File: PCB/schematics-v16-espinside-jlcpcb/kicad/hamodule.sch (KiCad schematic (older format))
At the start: 78 parts, among them J1 2604-1104, J10 EspSense, J11 Conn_01x02_Male, J2 2604-1102, J3 USB_B_Micro, J4 ESP Relays, J5 Current Jumper, J6 GND 3.3V, J7 Conn_01x02, J8 Current Jumper, J9 2604-1104, K1 PCN-105D, K2 PCN-105D, K3 PCN-105D, K4 PCN-105D, Q1 SS8050, Q2 SS8050, SW1 EN, SW2 IO0, U1 ULN2003A, U2 ESP32-WROOM-32D, U4 LD1117AV33_TO220, U5 MCP9700T-ETT, U6 LDA210-PDIP, U7 LDA210-PDIP, U8 CP2102N-A01-GQFN28

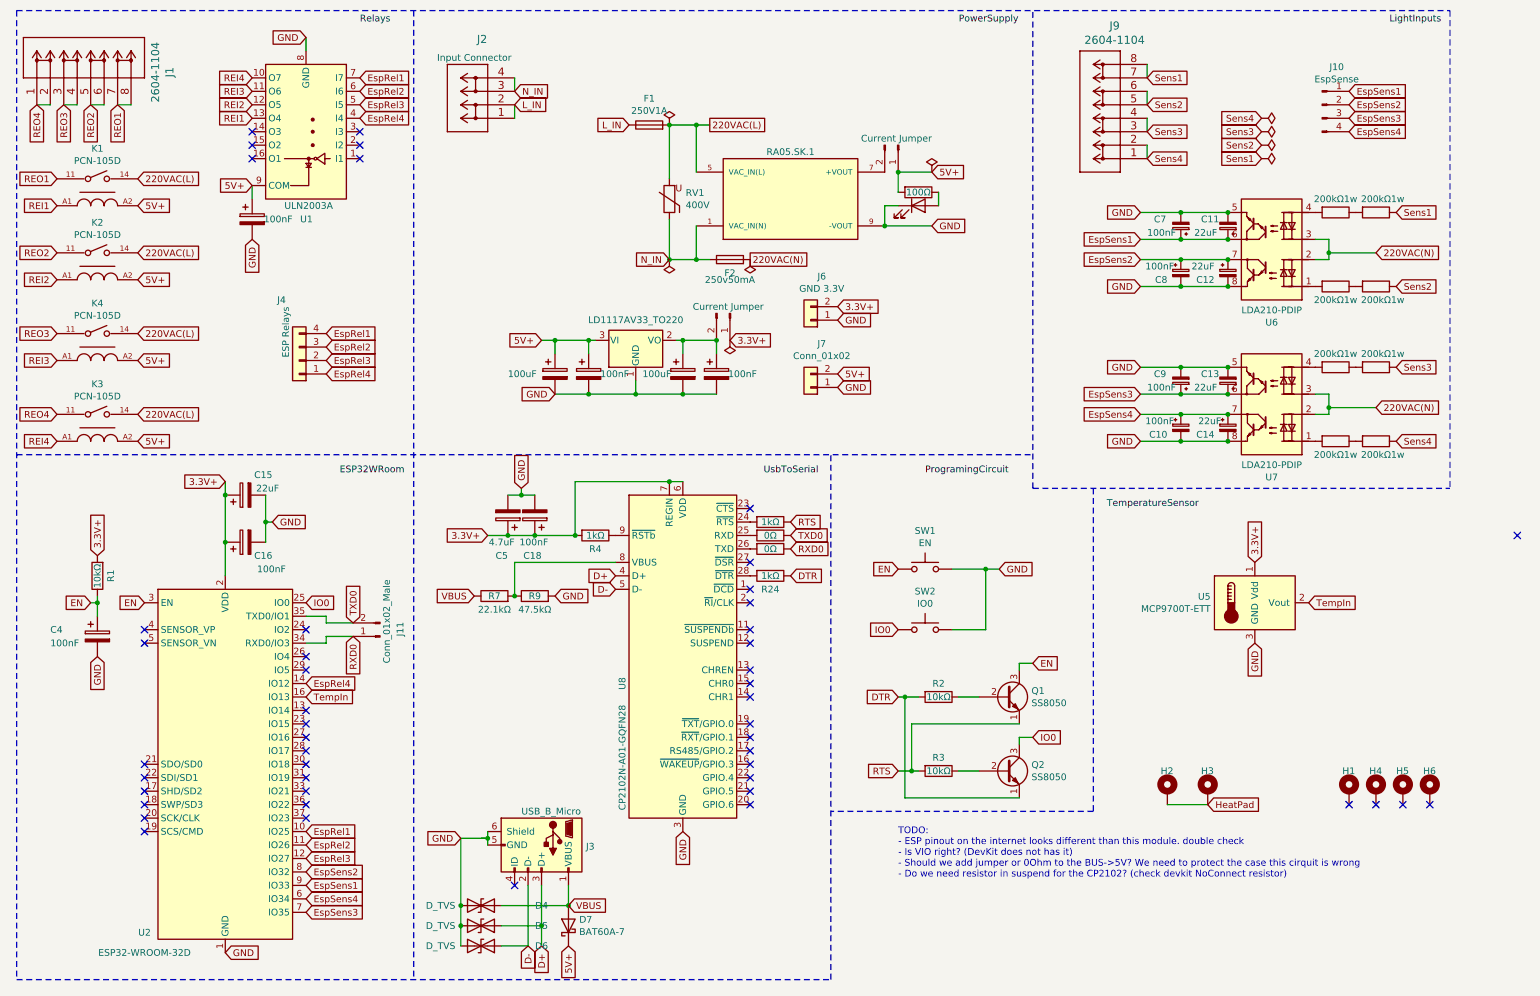
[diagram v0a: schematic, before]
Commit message: changed big caps + readme + routing + JLCPCB
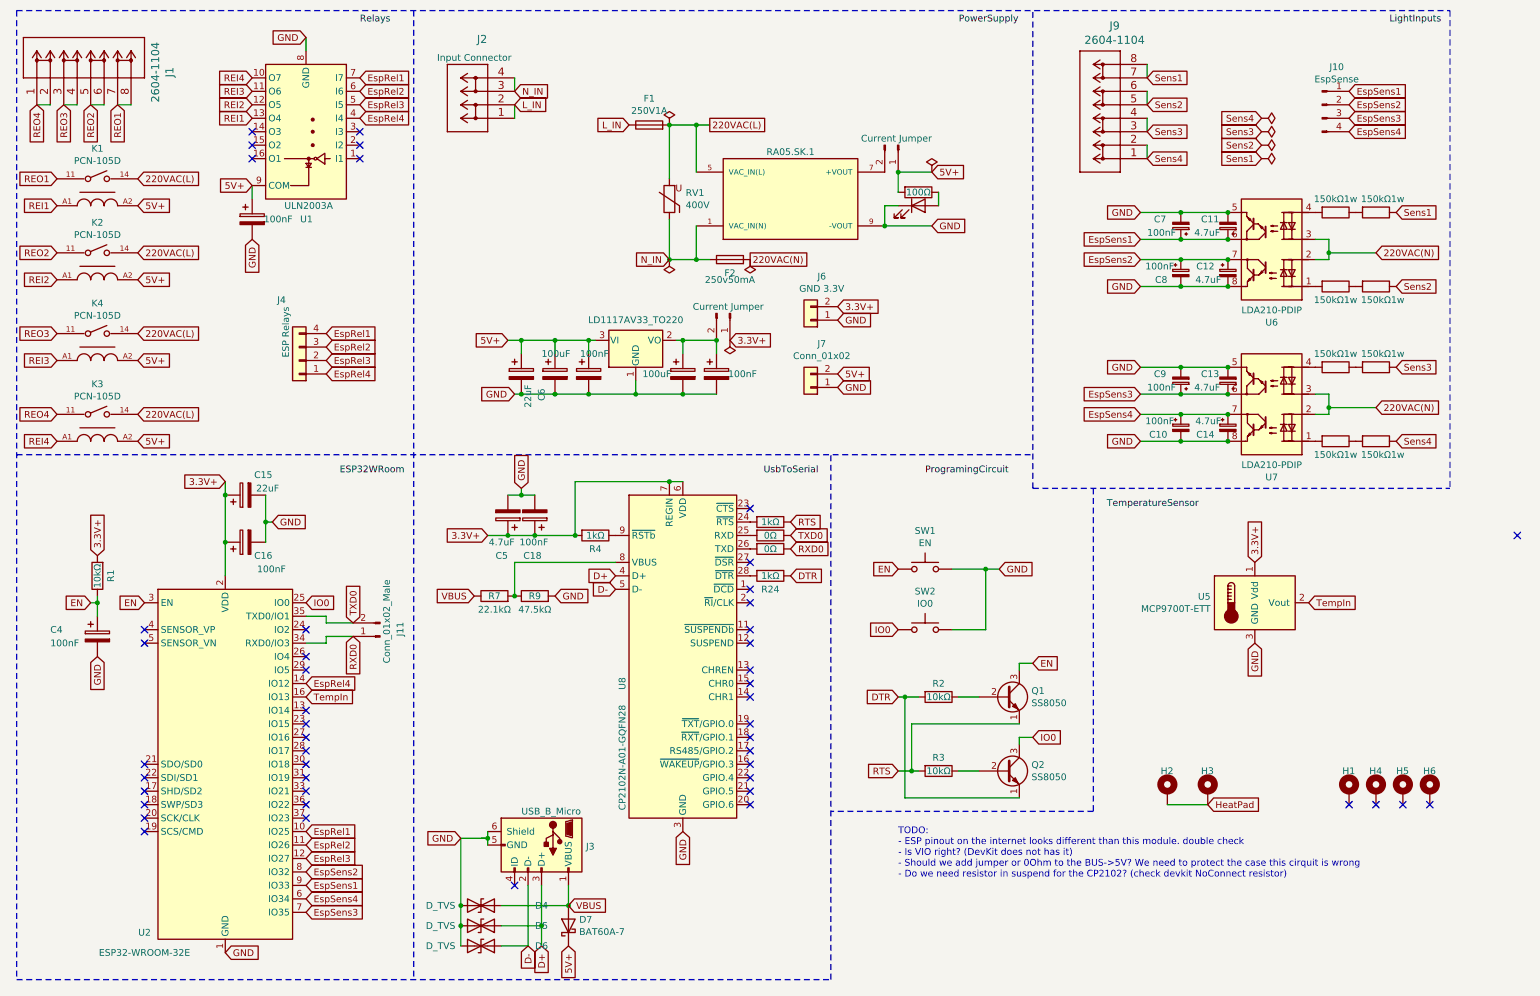
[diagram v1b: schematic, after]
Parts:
- added C6: 22uF, Capacitor_SMD:C_0603_1608Metric_Pad1.08x0.95mm_HandSolder, symbol Device:CP
- C11, C13, C14: value 22uF -> 4.7uF; footprint Capacitor_Tantalum_SMD:CP_EIA-3528-21_Kemet-B_Pad1.50x2.35mm_HandSolder -> Capacitor_SMD:C_1206_3216Metric_Pad1.42x1.75mm_HandSolder; JLCPCB C110051 -> C29823
- C12: value 22uF -> 4.7uF; footprint Capacitor_Tantalum_SMD:CP_EIA-3528-21_Kemet-B_Pad1.50x2.35mm_HandSolder -> Capacitor_SMD:C_1206_3216Metric_Pad1.42x1.75mm_HandSolder; JLCPCB C110051 -> C29823; Value (none) -> 4.7uF
- R16, R17, R18, R19, R20, R21, R22, R23: value 200kΩ1w -> 150kΩ1w; JLCPCB C38961 -> C25719
- U2: value ESP32-WROOM-32D -> ESP32-WROOM-32E; JLCPCB C701342 -> C701343
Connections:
- net 5V+: now also C6.1
- net GND: now also C6.2
